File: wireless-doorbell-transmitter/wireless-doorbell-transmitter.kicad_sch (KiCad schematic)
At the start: 14 parts, among them SW2 SW_Omron_B3FS, SW3 SW_DIP_x08, SW4 SW_DIP_x03, SW5 SW_Omron_B3FS, U1 L7805, U2 HT12E, U3 FS1000A 433MHz

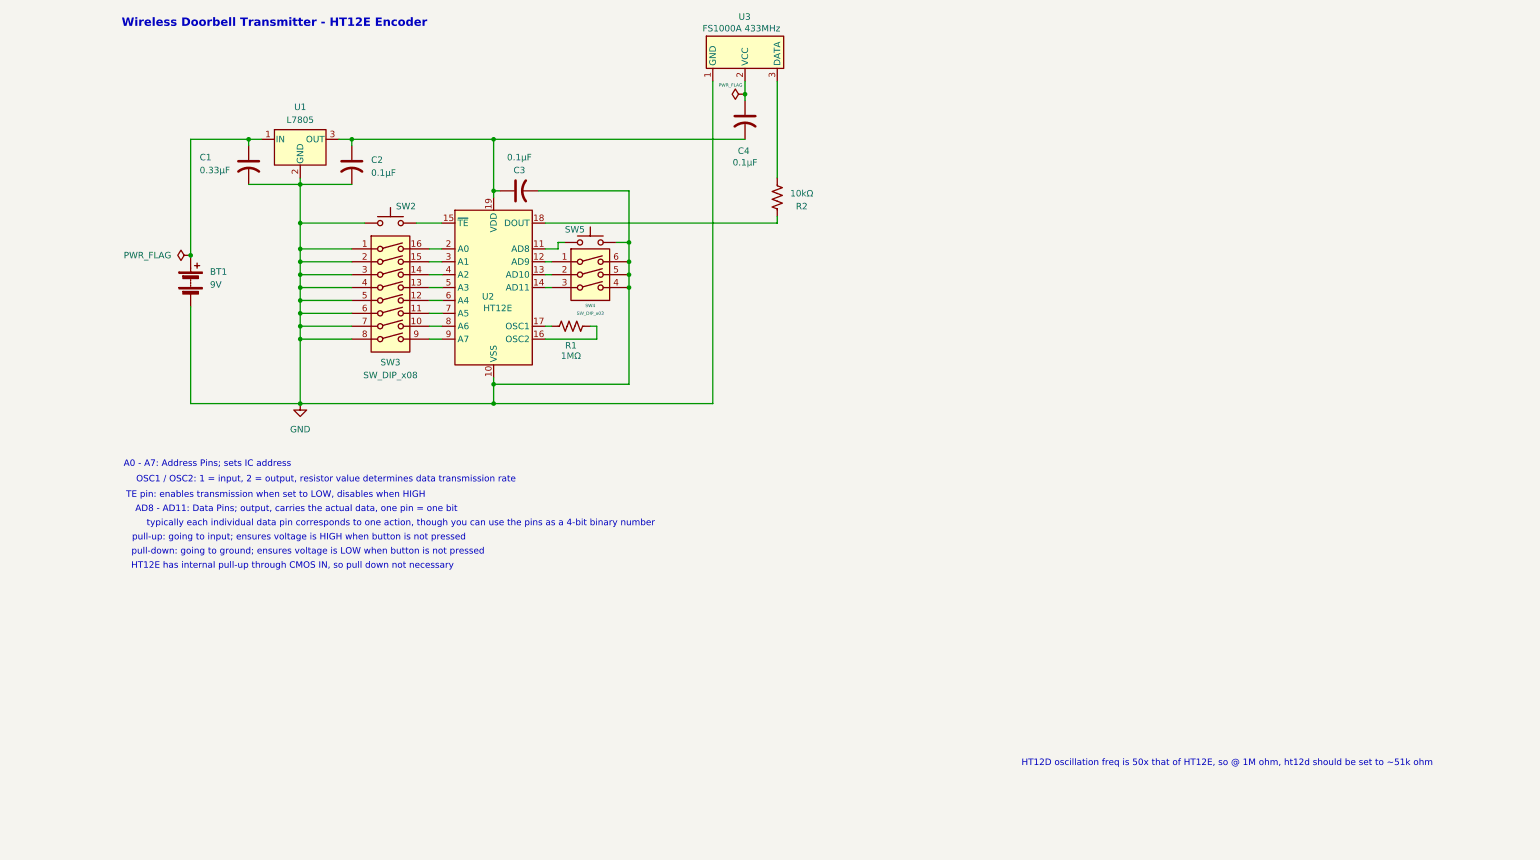
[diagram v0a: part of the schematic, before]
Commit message: This update added an ESP32-C3 MCU as well as an SC-SR501 PIR Sensor in order to give the doorbell a motion sensor along with a pushbutton switch as a backup.
Notable Changes:
• Added ESP32-C3 MCU

• Created & added custom symbol for SC-SR501 PIR Sensor

• Source voltage changed to 5V (previously 9V)

• Replaced 7805 IC with a TLV62568A-DRL 1-A 3.3V Buck Converter for voltage regulation across HT12E and ESP32-C3 MCU

• Re-wired ICs and FS1000A TX

Next Steps:

• Wire ESP32-C3 to HT12E data pins

• Re-wire unused DIP switches to data pins on HT12E

• Wire ESP32-C3 to PIR sensor
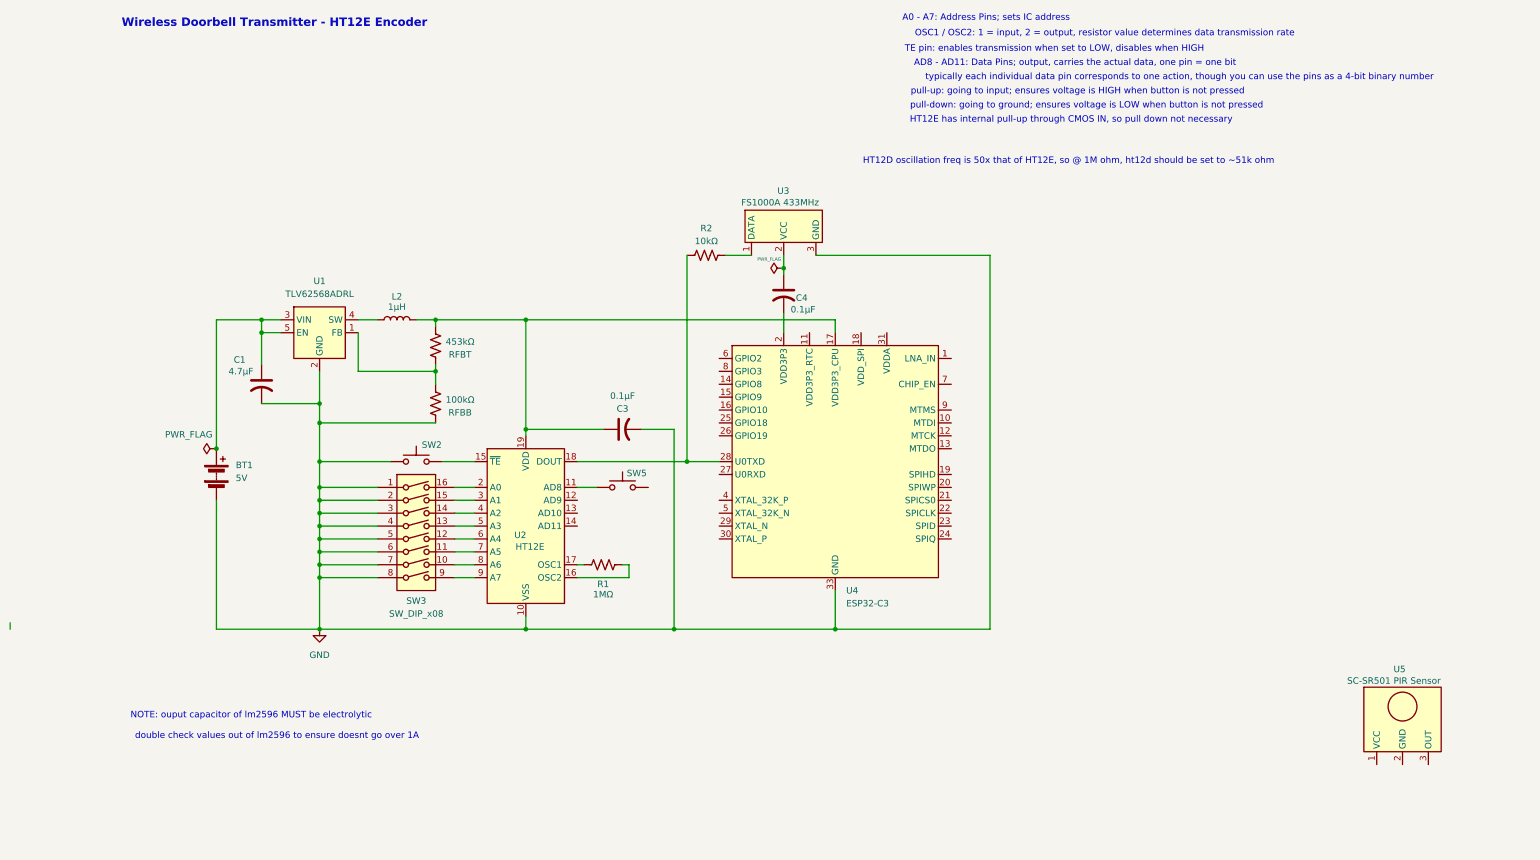
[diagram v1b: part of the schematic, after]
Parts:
- removed C2: 0.1μF, symbol Device:C_US
- removed SW4: SW_DIP_x03, symbol Switch:SW_DIP_x03
- removed U1: L7805, symbol Regulator_Linear:L7805
- added L2: 1μH, symbol Device:L
- added RFBB: 100kΩ, symbol Device:R_US
- added RFBT: 453kΩ, symbol Device:R_US
- added U1: TLV62568ADRL, Package_TO_SOT_SMD:SOT-563, symbol Regulator_Switching:TLV62568ADRL
- added U4: ESP32-C3, Package_DFN_QFN:QFN-32-1EP_5x5mm_P0.5mm_EP3.7x3.7mm, symbol MCU_Espressif:ESP32-C3
- added U5: SC-SR501 PIR Sensor, symbol PIR Sensor:HC-SR501
- BT1: value 9V -> 5V
- C1: value 0.33μF -> 4.7μF
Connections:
- net GND: now also U3.3 (GND), RFBB.2, U1.2 (GND), U4.33 (GND); no longer SW5.2, U3.1 (GND)
- net at R2.1: now also U3.1 (DATA); no longer U3.3 (DATA)
- net at R2.2, U2.18 (DOUT): now also U4.28 (U0TXD)
- net at C3.1, U2.19 (VDD): now also L2.2, RFBT.1, U4.17 (VDD3P3_CPU); no longer C4.2
- net at BT1.1 (+), C1.1: now also U1.3 (VIN), U1.5 (EN)
- new net: RFBB.1, RFBT.2, U1.1 (FB)
- new net: L2.1, U1.4 (SW)
- new net: C4.2, U4.2 (VDD3P3), U4.3 (VDD3P3)
- new net: U4.31 (VDDA), U4.32 (VDDA)
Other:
- note added: "NOTE: ouput capacitor of lm2596 MUST be electrolytic"
- note added: "double check values out of lm2596 to ensure doesnt go over 1A"
- moved on the sheet: BT1, C3, C4, R1, R2, SW2, SW3, SW5, U2, U3

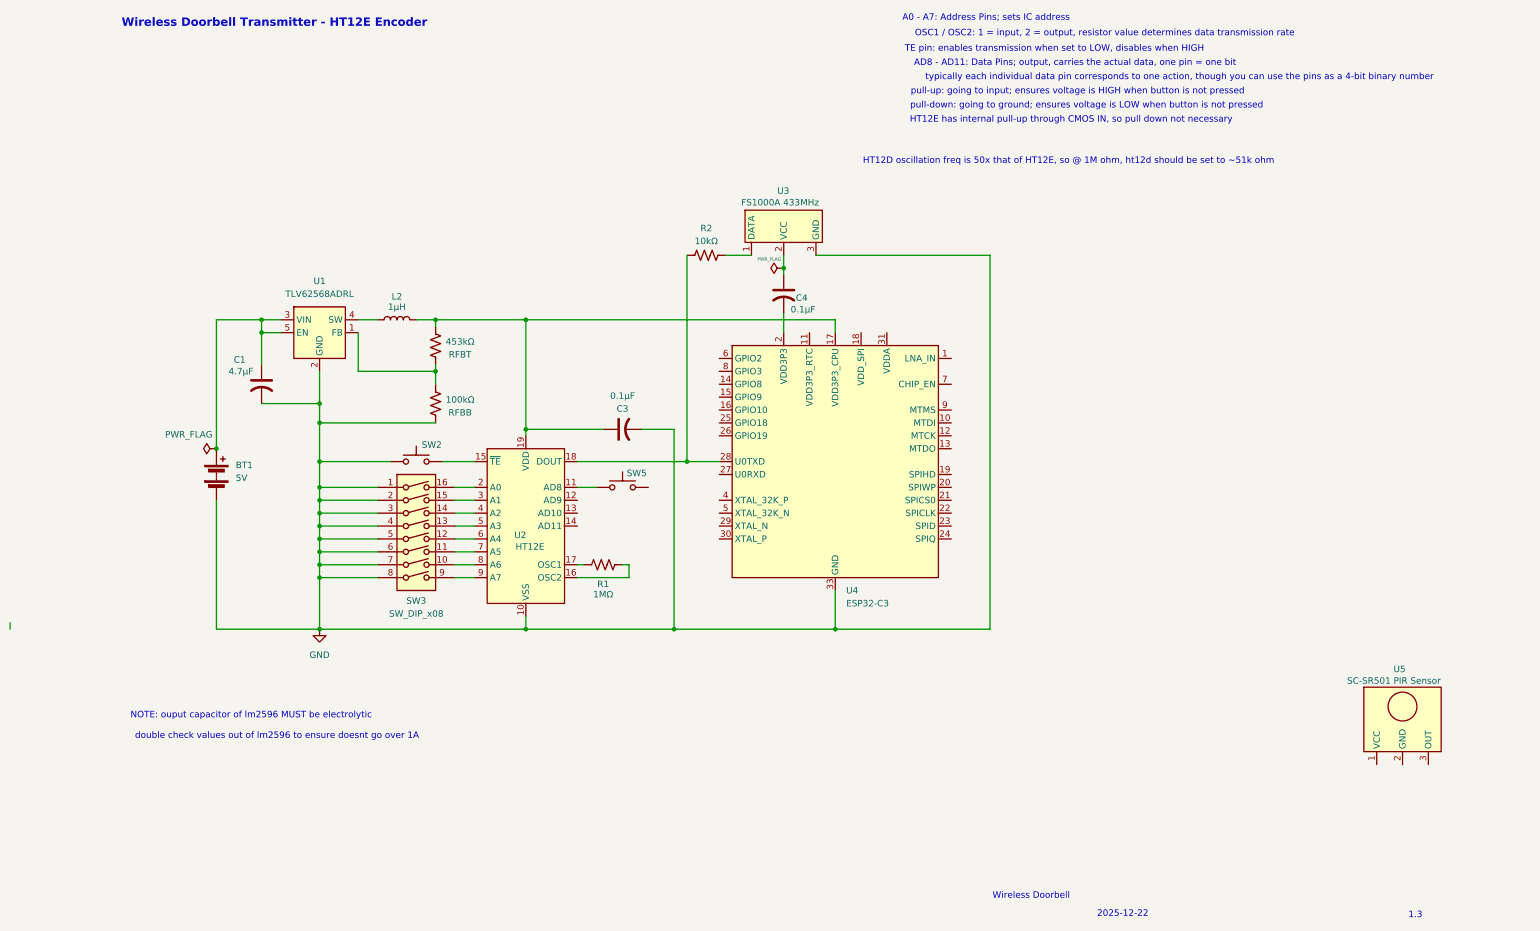
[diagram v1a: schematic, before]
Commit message: Improved Voltage Regulation and Circuit Protection - V1.2
• Added a small fuse for OC protection, as well as an SPST switch to act as a start/stop switch in case system needs to be turned off or restarted.

• Swapped TLV62568ADRL buck converter with a LM3671 3.3V Buck Converter Breakout module for easier installation.

To Do:

• Swap battery source with a li-ion 4.5V battery or keep at 5V and use a USB-C wall adapter for source (5V more efficient but limits placement); Li-ion requires PCM for protection and C script monitoring battery percentage so as to not drop below 3.0V

• Implement PIR Sensor
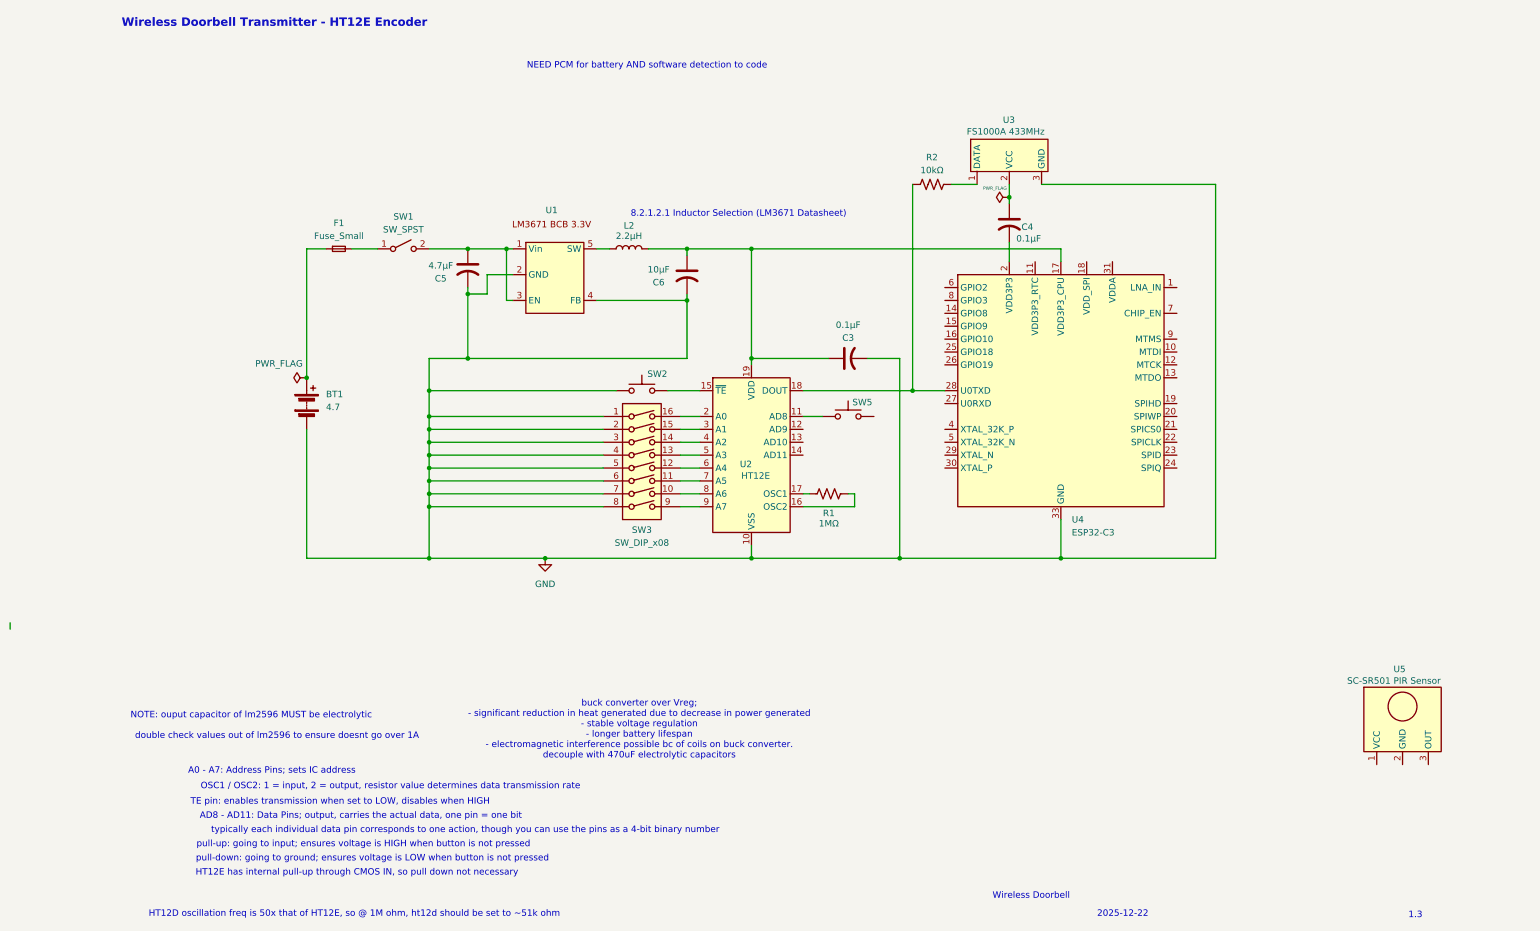
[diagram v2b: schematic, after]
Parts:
- removed C1: 4.7μF, symbol Device:C_US
- removed RFBB: 100kΩ, symbol Device:R_US
- removed RFBT: 453kΩ, symbol Device:R_US
- removed U1: TLV62568ADRL, Package_TO_SOT_SMD:SOT-563, symbol Regulator_Switching:TLV62568ADRL
- added C5: 4.7μF, symbol Device:C_US
- added C6: 10μF, symbol Device:C_US
- added F1: Fuse_Small, symbol Device:Fuse_Small
- added SW1: SW_SPST, symbol Switch:SW_SPST
- added U1: (no value), symbol Buck Converters:LM3671_3.3V
- BT1: value 5V -> 4.7
- L2: value 1μH -> 2.2μH
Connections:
- net GND: now also C5.2, C6.2, U1.2 (GND), U1.4 (FB)
- net at BT1.1 (+): now also F1.1
- net at L2.1: now also U1.5 (SW)
- net at C3.1, L2.2, U2.19 (VDD)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: now also C6.1
- new net: C5.1, SW1.2 (B), U1.1 (Vin), U1.3 (EN)
- new net: F1.2, SW1.1 (A)
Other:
- note added: "8.2.1.2.1 Inductor Selection (LM3671 Datasheet)"
- note added: "NEED PCM for battery AND software detection to code"
- note added: "buck converter over Vreg; - significant reduction in heat generated due to decrease in power generated - stable voltage regulation - longer battery lifespan - electromagnetic interference possible bc of coils on buck converter. decouple with 470uF electrolytic capacitors"
- moved on the sheet: BT1, C3, C4, L2, R1, R2, SW2, SW3, SW5, U2, U3, U4

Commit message: Architecture Improvements - V2.0
• Removed HT12E Encoder in order to use ESP32-C3 and RF module solely for serial communication

• Added and implemented HC-SR501 PIR Sensor to ESP32-C3

• Added nRF24L01+ RF module for SPI data transfer to future second PCB

• Separate page into flat schematic as well as modular sections for easier readability
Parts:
- removed C3: 0.1μF, symbol Device:C_US
- removed F1: Fuse_Small, symbol Device:Fuse_Small
- removed R1: 1MΩ, symbol Device:R_US
- removed R2: 10kΩ, symbol Device:R_US
- removed SW1: SW_SPST, symbol Switch:SW_SPST
- removed SW2, SW5: SW_Omron_B3FS, symbol Switch:SW_Omron_B3FS
- removed SW3: SW_DIP_x08, symbol Switch:SW_DIP_x08
- removed U2: HT12E, Package_SO:SOP-20_7.5x12.8mm_P1.27mm, symbol Interface:HT12E
- removed U3: FS1000A 433MHz, symbol RF-Transmitters:FS1000A_RF_433Mhz
- added Cin: 4.7μF, symbol Device:C_US
- added Cout: 10μF, symbol Device:C_US
- added L3: 2.2μH, symbol Device:L
- added U2: (no value), symbol Buck Converters:LM3671_3.3V
- added U6: SC-SR501 PIR Sensor, symbol PIR Sensor:HC-SR501
- added U7: ESP32-C3, Package_DFN_QFN:QFN-32-1EP_5x5mm_P0.5mm_EP3.7x3.7mm, symbol MCU_Espressif:ESP32-C3
- added U8: nRF24L01P, Package_DFN_QFN:QFN-20-1EP_4x4mm_P0.5mm_EP2.5x2.5mm, symbol RF:nRF24L01P
- BT1: value 4.7 -> Battery
- renumbered C5 to Cin, C6 to Cout
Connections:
- net GND: now also U6.2 (GND), U7.33 (GND), U8.14 (VSS), U8.17 (VSS), U8.20 (VSS), U8.8 (VSS); no longer BT1.2 (-), U1.4 (FB), U4.33 (GND)
- net +BATT: now reaches Cin.1, U1.1 (Vin), U1.3 (EN)
- net +BATT: now also U6.1 (VCC)
- net at U5.1 (VCC): now also BT1.1 (+), Cin.1, U2.1 (Vin), U2.3 (EN)
- net at U5.2 (GND): now also BT1.2 (-), U4.33 (GND), Cin.2, Cout.2
- net at U5.3 (OUT): now also U4.14 (GPIO8)
- net +3.3V: now reaches Cout.1, L2.2
- net +3.3V: now also U1.4 (FB), U7.17 (VDD3P3_CPU), U8.15 (VDD), U8.18 (VDD), U8.7 (VDD); no longer U4.17 (VDD3P3_CPU)
- net at U4.2 (VDD3P3), U4.3 (VDD3P3): no longer C4.2
- new net: Cout.1, L3.2, U2.4 (FB), U4.17 (VDD3P3_CPU)
- new net: L3.1, U2.5 (SW)
- new net: U7.14 (GPIO8), U8.1 (CE)
- new net: U7.21 (SPICS0), U8.2 (CSN)
- new net: U7.22 (SPICLK), U8.3 (SCK)
- new net: U7.23 (SPID), U8.4 (MOSI)
- new net: U7.24 (SPIQ), U8.5 (MISO)
- new net: U6.3 (OUT), U7.15 (GPIO9)
- new net: U7.2 (VDD3P3), U7.3 (VDD3P3)
- new net: U7.31 (VDDA), U7.32 (VDDA)
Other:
- note added: "***8.2.1.2.1 Inductor Selection (LM3671 Datasheet)"
- note added: "3.3V Buck Converter"
- note removed: "8.2.1.2.1 Inductor Selection (LM3671 Datasheet)"
- moved on the sheet: C4, Cin, Cout, L2, U1, U4, U5
